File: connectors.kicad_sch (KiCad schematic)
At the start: 42 parts, among them J6 10107844-002LF, J8 JST_XH_1x2_B2B-XH-A-LF-SN, SW1 MSS3-V-T_R, U11 USB-C_GCT_USB4145-03-0070-C

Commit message: Updated project with corrcted USBC
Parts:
- U11: footprint antmicro-footprints:GCT_USB4145-03-0070-C_REVA -> antmicro-footprints:USB-C_Receptacle_GCT_USB4145-03-0070-C
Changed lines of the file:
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@@
     (pin "1")
+  )
+  (symbol (lib_name "USB-C_GCT_USB4145-03-0070-C_1") (lib_id "antmicroUSBConnectors:USB-C_GCT_USB4145-03-0070-C") (at 328.93 124.46 0) (unit 1)
+    (in_bom yes) (on_board yes) (fields_autoplaced)
+    (property "Reference" "U11" (id 0) (at 342.9 115.57 0)
+      (effects (font (size 1.27 1.27) (thickness 0.15)))
+    )
+    (property "Value" "USB-C_GCT_USB4145-03-0070-C" (id 1) (at 372.11 132.08 0)
+      (effects (font (size 1.27 1.27) (thickness 0.15)) (justify left bottom) hide)
+    )
+    (property "Footprint" "antmicro-footprints:USB-C_Receptacle_GCT_USB4145-03-0070-C" (id 2) (at 372.11 134.62 0)
+      (effects (font (size 1.27 1.27) (thickness 0.15)) (justify left bottom) hide)
+    )
+    (property "Datasheet" "https://gct.co/files/drawings/usb4145.pdf" (id 3) (at 372.11 137.16 0)
+      (effects (font (size 1.27 1.27) (thickness 0.15)) (justify left bottom) hide)
+    )
+    (property "MPN" "USB4145-03-0070-C" (id 4) (at 342.9 118.11 0)
+      (effects (font (size 1.27 1.27) (thickness 0.15)))
+    )
+    (property "Manufacturer" "GCT" (id 5) (at 372.11 139.7 0)
+      (effects (font (size 1.27 1.27) (thickness 0.15)) (justify left bottom) hide)
+    )
+    (property "License" "Apache-2.0" (id 6) (at 372.11 142.24 0)
+      (effects (font (size 1.27 1.27) (thickness 0.15)) (justify left bottom) hide)
+    )
+    (property "Author" "Antmicro" (id 7) (at 372.11 144.78 0)
+      (effects (font (size 1.27 1.27) (thickness 0.15)) (justify left bottom) hide)
+    )
+    (pin "A12")
+    (pin "A5")
+    (pin "A6")
+    (pin "A7")
+    (pin "A8")
+    (pin "A9")
+    (pin "B12")
+    (pin "B5")
+    (pin "B6")
+    (pin "B7")
+    (pin "B8")
+    (pin "B9")
+    (pin "S2")
   )
   (symbol (lib_name "PESD5V0S2BQA_1") (lib_id "antmicroTVSDiodes:PESD5V0S2BQA") (at 303.53 151.13 0) (unit 1)
@@
     (pin "3")
   )
-  (symbol (lib_id "antmicroUSBConnectors:USB-C_GCT_USB4145-03-0070-C") (at 328.93 124.46 0) (unit 1)
-    (in_bom yes) (on_board yes) (fields_autoplaced)
-    (property "Reference" "U11" (id 0) (at 342.9 115.57 0)
-      (effects (font (size 1.27 1.27) (thickness 0.15)))
-    )
-    (property "Value" "USB-C_GCT_USB4145-03-0070-C" (id 1) (at 372.11 132.08 0)
-      (effects (font (size 1.27 1.27) (thickness 0.15)) (justify left bottom) hide)
-    )
-    (property "Footprint" "antmicro-footprints:GCT_USB4145-03-0070-C_REVA" (id 2) (at 372.11 134.62 0)
-      (effects (font (size 1.27 1.27) (thickness 0.15)) (justify left bottom) hide)
-    )
-    (property "Datasheet" "https://gct.co/files/drawings/usb4145.pdf" (id 3) (at 372.11 137.16 0)
-      (effects (font (size 1.27 1.27) (thickness 0.15)) (justify left bottom) hide)
-    )
-    (property "MPN" "USB4145-03-0070-C" (id 4) (at 342.9 118.11 0)
-      (effects (font (size 1.27 1.27) (thickness 0.15)))
-    )
-    (property "Manufacturer" "GCT" (id 5) (at 372.11 139.7 0)
-      (effects (font (size 1.27 1.27) (thickness 0.15)) (justify left bottom) hide)
-    )
-    (property "License" "Apache-2.0" (id 6) (at 372.11 142.24 0)
-      (effects (font (size 1.27 1.27) (thickness 0.15)) (justify left bottom) hide)
-    )
-    (property "Author" "Antmicro" (id 7) (at 372.11 144.78 0)
-      (effects (font (size 1.27 1.27) (thickness 0.15)) (justify left bottom) hide)
-    )
-    (pin "A12")
-    (pin "A5")
-    (pin "A6")
-    (pin "A7")
-    (pin "A8")
-    (pin "A9")
-    (pin "B12")
-    (pin "B5")
-    (pin "B6")
-    (pin "B7")
-    (pin "B8")
-    (pin "B9")
-    (pin "S2")
-  )
   (symbol (lib_name "R_0R_0402_2") (lib_id "antmicroResistors0402:R_0R_0402") (at 194.31 143.51 0) (unit 1)

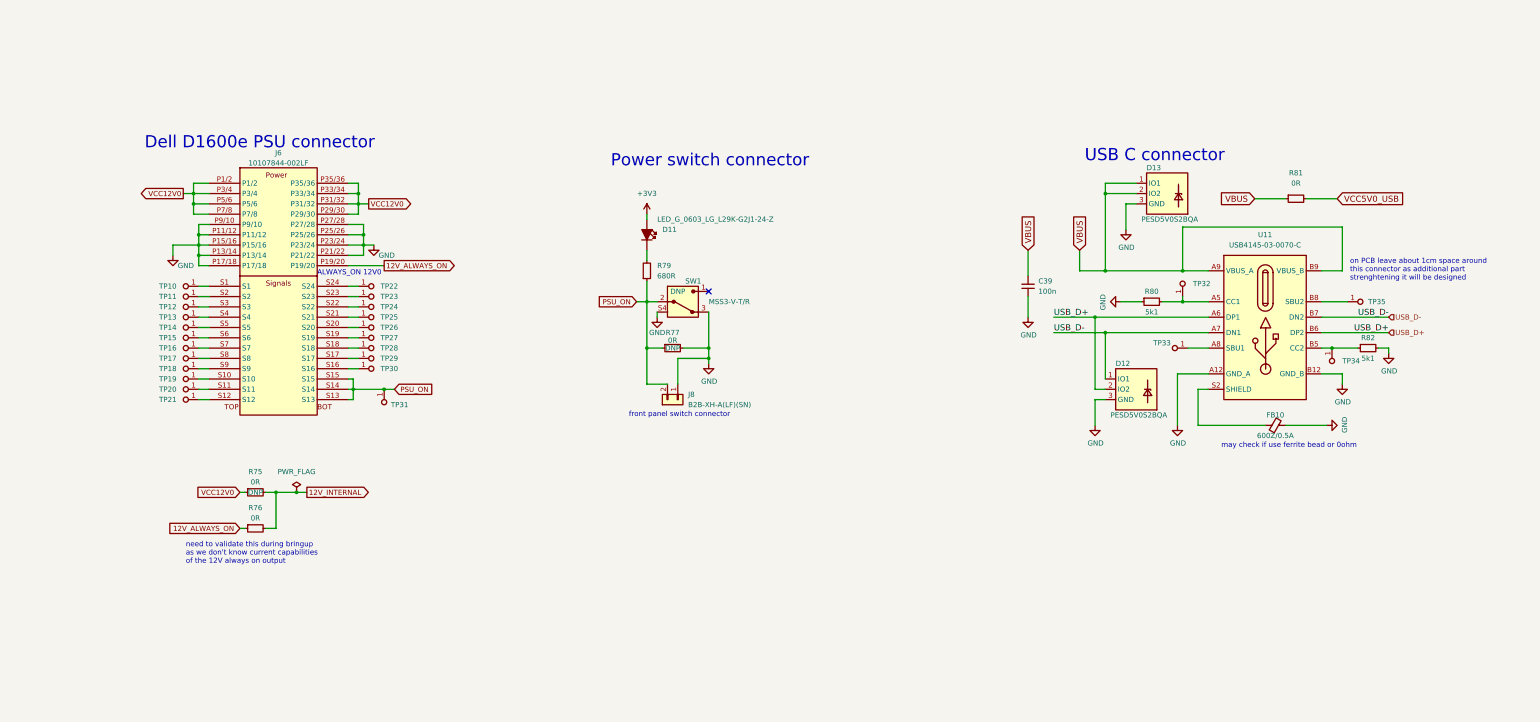
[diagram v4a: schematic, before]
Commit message: Placement of supply section on PCB
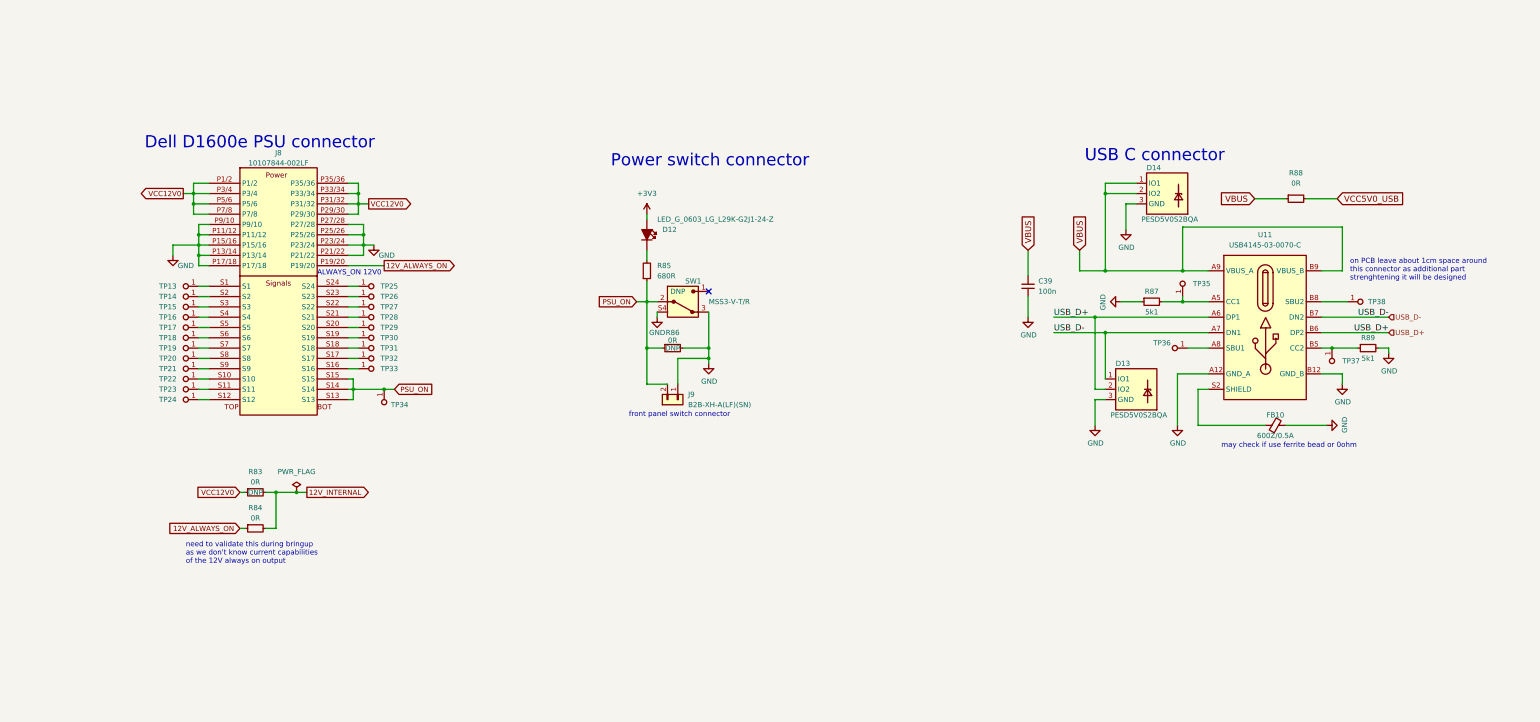
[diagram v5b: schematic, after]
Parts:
- renumbered D11 to D12, D12 to D13, D13 to D14, J6 to J8, J8 to J9, R75 to R83, R76 to R84, R79 to R85, R77 to R86, R80 to R87, R81 to R88, R82 to R89, TP10 to TP13, TP11 to TP14, TP12 to TP15, TP13 to TP16, TP14 to TP17, TP15 to TP18, TP16 to TP19, TP17 to TP20, TP18 to TP21, TP19 to TP22, TP20 to TP23, TP21 to TP24, TP22 to TP25, TP23 to TP26, TP24 to TP27, TP25 to TP28, TP26 to TP29, TP27 to TP30, TP28 to TP31, TP29 to TP32, TP30 to TP33, TP31 to TP34, TP32 to TP35, TP33 to TP36, TP34 to TP37, TP35 to TP38

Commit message: Implement changes suggested in schematic review
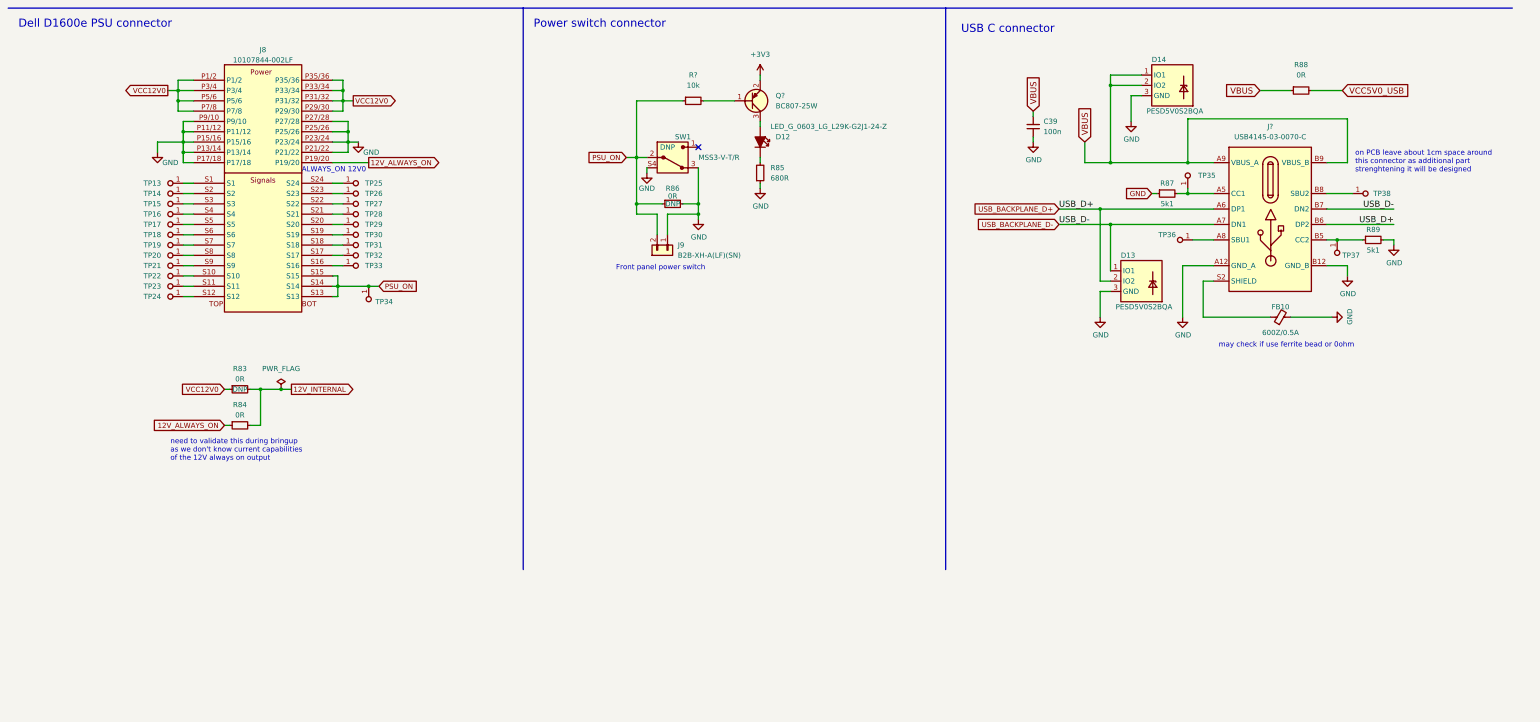
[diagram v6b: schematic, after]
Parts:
- removed U11: USB-C_GCT_USB4145-03-0070-C, antmicro-footprints:USB-C_Receptacle_GCT_USB4145-03-0070-C, symbol antmicroUSBConnectors:USB-C_GCT_USB4145-03-0070-C
- added J?: USB-C_GCT_USB4145-03-0070-C, antmicro-footprints:USB-C_Receptacle_GCT_USB4145-03-0070-C, symbol antmicroUSBConnectors:USB-C_GCT_USB4145-03-0070-C
- added Q?: BC807-25W, antmicro-footprints:SOT-323, symbol antmicroTransistorsBipolarSingle:BC807-25W
- added R?: R_10k_0402, antmicro-footprints:R_0402_1005Metric, symbol antmicroResistors0402:R_10k_0402
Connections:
- net +3V3: now also Q?.2; no longer D12.1
- net GND: now also R85.1, J?.A12 (GND_A), J?.B12 (GND_B)
- net PSU_ON: now also R?.1; no longer R85.1
- net VBUS: now also J?.A9 (VBUS_A), J?.B9 (VBUS_B)
- net at TP38.1: now also J?.B8 (SBU2)
- net at R87.2, TP35.1: now also J?.A5 (CC1)
- net at TP36.1: now also J?.A8 (SBU1)
- net at R89.1, TP37.1: now also J?.B5 (CC2)
- net at FB10.1: now also J?.S2 (SHIELD)
- net USB_D+ renamed USB_BACKPLANE_D+
- net USB_BACKPLANE_D+: now also J?.A6 (DP1), J?.B6 (DP2)
- net USB_D- renamed USB_BACKPLANE_D-
- net USB_BACKPLANE_D-: now also J?.A7 (DN1), J?.B7 (DN2)
- new net: D12.1, Q?.3
- new net: Q?.1, R?.2
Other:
- note added: "Front panel power switch"
- note removed: "front panel switch connector"
- company: (none) -> Antmicro Ltd
- moved on the sheet: C39, D12, D13, D14, FB10, J8, J9, R83, R84, R85, R86, R87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

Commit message: 2nd part of review changes
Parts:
- added D45: ESDA25P35-1U1M, antmicro-footprints:ESDA25P35-1U1M, symbol antmicroTVSDiodes:ESDA25P35-1U1M
- gave numbers to parts that had none: 3
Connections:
- net GND: now also D45.1 (K)
- net PSU_ON: now also D45.2 (A)
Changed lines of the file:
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@@
   (junction (at 74.93 80.01) (diameter 0) (color 0 0 0 0)
   )
+  (junction (at 193.04 82.55) (diameter 0) (color 0 0 0 0)
+  )
   (junction (at 323.85 105.41) (diameter 0) (color 0 0 0 0)
   )
@@
     (stroke (width 0) (type default) (color 0 0 0 0))
   )
+  (wire (pts (xy 193.04 82.55) (xy 187.96 82.55))
+    (stroke (width 0) (type default) (color 0 0 0 0))
+  )
   (wire (pts (xy 72.39 80.01) (xy 74.93 80.01))
     (stroke (width 0) (type default) (color 0 0 0 0))
@@
     (stroke (width 0) (type default) (color 0 0 0 0))
   )
-  (wire (pts (xy 199.39 82.55) (xy 187.96 82.55))
+  (wire (pts (xy 199.39 82.55) (xy 193.04 82.55))
     (stroke (width 0) (type default) (color 0 0 0 0))
   )
@@
     )
   )
+  (global_label "GND" (shape input) (at 149.86 151.13 90) (fields_autoplaced)
+    (effects (font (size 1.27 1.27)) (justify left))
+    (property "Intersheet References" "${INTERSHEET_REFS}" (id 0) (at 149.7806 144.9353 90)
+      (effects (font (size 1.27 1.27)) (justify left) hide)
+    )
+  )
   (global_label "PSU_ON" (shape input) (at 185.42 96.52 180) (fields_autoplaced)
     (effects (font (size 1.27 1.27)) (justify right))
@@
     (pin "3")
   )
+  (symbol (lib_id "antmicroTVSDiodes:ESDA25P35-1U1M") (at 193.04 87.63 90) (unit 1)
+    (in_bom yes) (on_board yes)
+    (property "Reference" "D45" (id 0) (at 194.945 84.455 90)
+      (effects (font (size 1.27 1.27) (thickness 0.15)) (justify right))
+    )
+    (property "Value" "ESDA25P35-1U1M" (id 1) (at 194.945 86.36 90)
+      (effects (font (size 1.27 1.27) (thickness 0.15)) (justify right))
+    )
+    (property "Footprint" "antmicro-footprints:ESDA25P35-1U1M" (id 2) (at 203.2 63.5 0)
+      (effects (font (size 1.27 1.27) (thickness 0.15)) (justify left bottom) hide)
+    )
+    (property "Datasheet" "https://www.st.com/resource/en/datasheet/esda25p35-1u1m.pdf" (id 3) (at 205.74 63.5 0)
+      (effects (font (size 1.27 1.27) (thickness 0.15)) (justify left bottom) hide)
+    )
+    (property "MPN" "ESDA25P35-1U1M" (id 4) (at 208.28 63.5 0)
+      (effects (font (size 1.27 1.27) (thickness 0.15)) (justify left bottom) hide)
+    )
+    (property "Manufacturer" "STMicroelectronics" (id 5) (at 210.82 63.5 0)
+      (effects (font (size 1.27 1.27) (thickness 0.15)) (justify left bottom) hide)
+    )
+    (property "Author" "Antmicro" (id 6) (at 213.36 63.5 0)
+      (effects (font (size 1.27 1.27) (thickness 0.15)) (justify left bottom) hide)
+    )
+    (property "License" "Apache-2.0" (id 7) (at 215.9 63.5 0)
+      (effects (font (size 1.27 1.27) (thickness 0.15)) (justify left bottom) hide)
+    )
+    (pin "1")
+    (pin "2")
+  )
   (symbol (lib_name "R_0R_0402_2") (lib_id "antmicroResistors0402:R_0R_0402") (at 194.31 107.95 0) (unit 1)
     (in_bom yes) (on_board yes)
@@
   (symbol (lib_id "antmicroResistors0402:R_10k_0402") (at 199.39 82.55 0) (unit 1)
     (in_bom yes) (on_board yes) (fields_autoplaced)
-    (property "Reference" "R?" (id 0) (at 201.93 76.2 0)
+    (property "Reference" "R301" (id 0) (at 201.93 76.2 0)
       (effects (font (size 1.27 1.27) (thickness 0.15)))
     )
@@
     (pin "1")
   )
+  (symbol (lib_id "antmicropower:GND") (at 193.04 87.63 0) (unit 1)
+    (in_bom yes) (on_board yes)
+    (property "Reference" "#PWR0214" (id 0) (at 193.04 93.98 0)
+      (effects (font (size 1.27 1.27)) hide)
+    )
+    (property "Value" "GND" (id 1) (at 196.85 88.9 0))
+    (property "Footprint" "" (id 2) (at 193.04 87.63 0)
+      (effects (font (size 1.27 1.27)) hide)
+    )
+    (property "Datasheet" "" (id 3) (at 193.04 87.63 0)
+      (effects (font (size 1.27 1.27)) hide)
+    )
+    (pin "1")
+  )
   (symbol (lib_id "antmicropower:PWR_FLAG") (at 100.33 153.67 0) (unit 1)
     (in_bom yes) (on_board yes) (fields_autoplaced)
@@
   (symbol (lib_id "antmicroUSBConnectors:USB-C_GCT_USB4145-03-0070-C") (at 330.2 97.79 0) (unit 1)
     (in_bom yes) (on_board yes) (fields_autoplaced)
-    (property "Reference" "J?" (id 0) (at 344.17 88.9 0)
+    (property "Reference" "J10" (id 0) (at 344.17 88.9 0)
       (effects (font (size 1.27 1.27) (thickness 0.15)))
     )
@@
   (symbol (lib_id "antmicroTransistorsBipolarSingle:BC807-25W") (at 212.09 82.55 0) (mirror x) (unit 1)
     (in_bom yes) (on_board yes) (fields_autoplaced)
-    (property "Reference" "Q?" (id 0) (at 222.25 81.2799 0)
+    (property "Reference" "Q29" (id 0) (at 222.25 81.2799 0)
       (effects (font (size 1.27 1.27) (thickness 0.15)) (justify left))
     )
@@
     (pin "1")
   )
+  (symbol (lib_id "power:GND") (at 149.86 151.13 0) (mirror y) (unit 1)
+    (in_bom yes) (on_board yes)
+    (property "Reference" "#PWR0142" (id 0) (at 149.86 157.48 0)
+      (effects (font (size 1.27 1.27)) hide)
+    )
+    (property "Value" "GND" (id 1) (at 156.21 152.4 0)
+      (effects (font (size 1.27 1.27)) (justify left))
+    )
+    (property "Footprint" "" (id 2) (at 149.86 151.13 0)
+      (effects (font (size 1.27 1.27)) hide)
+    )
+    (property "Datasheet" "" (id 3) (at 149.86 151.13 0)
+      (effects (font (size 1.27 1.27)) hide)
+    )
+    (pin "1")
+  )
   (symbol (lib_id "antmicroTestPoints:TP_1mm_SMD") (at 121.92 128.27 270) (unit 1)
     (in_bom yes) (on_board yes)
@@
   (symbol (lib_id "antmicropower:GND") (at 218.44 104.14 0) (unit 1)
     (in_bom yes) (on_board yes)
-    (property "Reference" "#PWR?" (id 0) (at 218.44 110.49 0)
+    (property "Reference" "#PWR0253" (id 0) (at 218.44 110.49 0)
       (effects (font (size 1.27 1.27)) hide)
     )
